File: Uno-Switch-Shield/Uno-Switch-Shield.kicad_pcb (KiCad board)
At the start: 2 copper layers, 68.6 x 53.3 mm, 30 parts, among them P1 Power, P10 CONN_01X10, P11 CONN_01X10, P12 CONN_01X10, P2 Analog, P3 Digital, P4 Digital, P5 CONN_01X01, P6 CONN_01X01, P7 CONN_01X01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

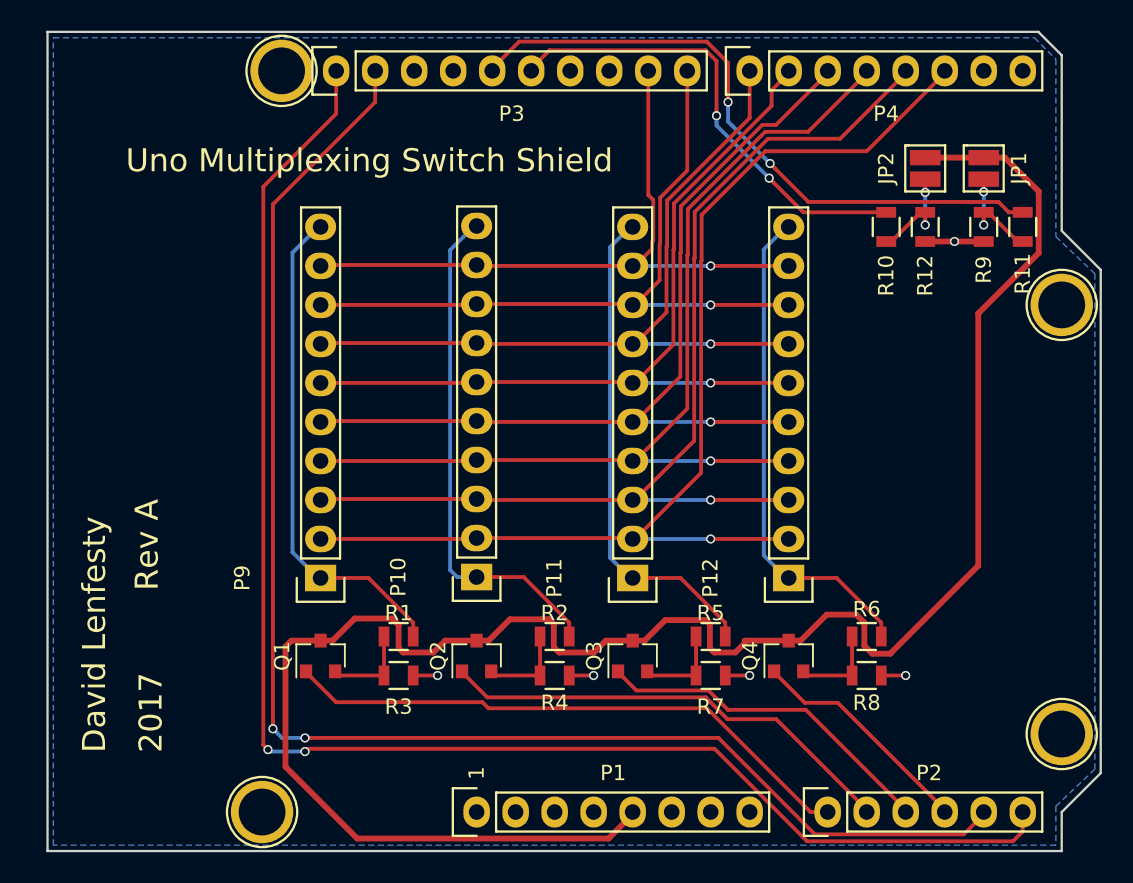
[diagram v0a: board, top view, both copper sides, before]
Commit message: Made the Uno Switch Shield six headers instead of four. Also some re-exporting of gerbers.
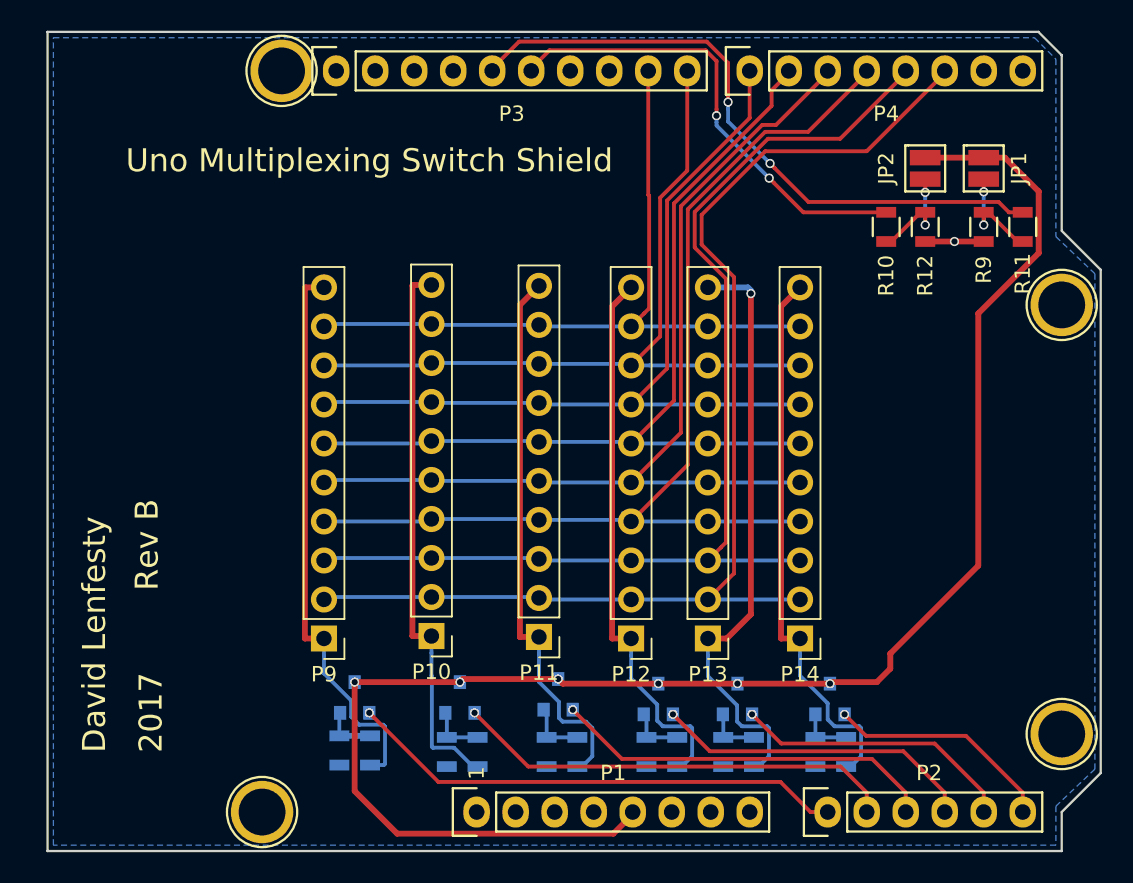
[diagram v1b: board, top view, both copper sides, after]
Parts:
- added P13: CONN_01X10, Socket_Strips:Socket_Strip_Straight_1x10_Pitch2.54mm, F.Cu at (154.0, 112.5)
- added P14: CONN_01X10, Socket_Strips:Socket_Strip_Straight_1x10_Pitch2.54mm, F.Cu at (160.0, 112.5)
- added Q5: Q_NPN_BEC, TO_SOT_Packages_SMD:SOT-23, B.Cu at (155.9, 116.5)
- added Q6: Q_NPN_BEC, TO_SOT_Packages_SMD:SOT-23, B.Cu at (161.9, 116.5)
- added R13: 1K, Resistors_SMD:R_0805, B.Cu at (157.0, 119.9)
- added R14: 1K, Resistors_SMD:R_0805, B.Cu at (163.0, 119.9)
- added R15: 10K, Resistors_SMD:R_0805, B.Cu at (155.0, 119.9)
- added R16: 10K, Resistors_SMD:R_0805, B.Cu at (161.0, 119.9)
- P10, P11, P12, P9: footprint Socket_Strips:Socket_Strip_Straight_1x10 -> Socket_Strips:Socket_Strip_Straight_1x10_Pitch2.54mm
- Q1, Q2, Q3, Q4, R1, R2, R3, R4, R5, R6, R7, R8: moved to B.Cu
- moved R8 15.2 mm to (150.0, 119.9), turned to 270 degrees
- moved R6 14.5 mm to (152.0, 119.9), turned to 270 degrees
- moved R7 11.8 mm to (143.5, 119.9), turned to 270 degrees
- moved R5 11.5 mm to (145.5, 119.9), turned to 270 degrees
- moved P12 11.0 mm to (149.0, 112.5), turned to 180 degrees
- moved R2 9.04 mm to (139.0, 119.9), turned to 270 degrees
- moved Q4 8.94 mm to (150.8, 116.5)
- moved R4 8.61 mm to (137.0, 119.9), turned to 270 degrees
- moved R1 7.65 mm to (132.0, 119.8), turned to 270 degrees
- moved P11 7.21 mm to (143.0, 112.4), turned to 180 degrees
- moved R3 6.22 mm to (130.0, 119.8), turned to 270 degrees
- moved Q3 5.46 mm to (144.2, 116.2)
- moved P10 4.84 mm to (136.0, 112.4), turned to 180 degrees
- moved P9 3.95 mm to (129.0, 112.5), turned to 180 degrees
- moved Q1 3.50 mm to (131.0, 116.4)
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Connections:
- P3 pad 1: /A5(SCL) -> Net-(P3-Pad1)
- P3 pad 2: /A4(SDA) -> Net-(P3-Pad2)
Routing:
- net /A5(SCL): track 99.6 -> 15.0 mm, vias 2 -> 1
- net /A4(SDA): track 95.4 -> 18.5 mm, vias 2 -> 1
- net Net-(P13-Pad1): track 0.00 -> 39.3 mm, vias 0 -> 1
- net Net-(P14-Pad1): track 0.00 -> 36.4 mm
- net +5V: track 125.9 -> 106.7 mm, vias 0 -> 6
- net GND: track 10.2 -> 3.81 mm, vias 5 -> 1
- net /A3: track 15.0 -> 21.2 mm, vias 0 -> 1
- net /4: track 64.0 -> 69.8 mm, vias 1 -> 0
- net /A0: track 37.8 -> 32.5 mm, vias 0 -> 1
- net /2: track 73.4 -> 78.3 mm, vias 1 -> 0
- net /3(**): track 68.7 -> 73.5 mm, vias 1 -> 0
- net /5(**): track 59.3 -> 63.9 mm, vias 1 -> 0
- net /8: track 47.3 -> 51.8 mm, vias 1 -> 0
- net /6(**): track 55.1 -> 59.6 mm, vias 1 -> 0
- net /7: track 51.6 -> 56.1 mm, vias 1 -> 0
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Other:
- board text added: "Rev B"
- board text removed: "Rev A"
